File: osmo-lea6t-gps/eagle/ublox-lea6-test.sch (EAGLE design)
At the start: 48 parts, among them U1 UBLOX-LEA-6T, U2 TPS73633, U3 TPS73633, X1 SERIAL, X2 ANT, X3 FOUT, X4 ANT, X5 FOUT, X6 1PPS, X7 PC, X8 1PPS, X9 22-23-2021

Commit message: sylvains branch (ignores some of harald's changes)
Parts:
- added LED1: (no value), led:LEDSML0603
- added R13: (no value), we_passive:R-EU_0603
- added R14: DNP, we_passive:R-EU_0603
- added TP8: TESTPAD, we_conn:TESTPAD
- C10, C6: value 10u -> (none)
- C11, C13, C7, C9: value 1u -> ?
- C12, C8: value 10n -> ?
- D1, D2: value BAT54 -> (none)
- R10: value 1k -> OR
- R12: value DNP -> (none)
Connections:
- new net N$27: LED1.C, R13.2
- new net N$28: R14.1, TP8.TP
- net 3V3: now also LED1.A
- net GND: now also R13.1
- net N$6: now also R14.2
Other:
- moved on the sheet: C6, D2
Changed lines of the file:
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@@
 <?xml version="1.0" encoding="utf-8"?>
 <!DOCTYPE eagle SYSTEM "eagle.dtd">
-<eagle version="6.0">
+<eagle version="6.1">
 <drawing>
 <settings>
@@
 <setting verticaltext="up"/>
 </settings>
-<grid distance="0.1" unitdist="inch" unit="inch" style="lines" multiple="1" display="no" altdistance="0.01" altunitdist="inch" altunit="inch"/>
+<grid distance="0.1" unitdist="inch" unit="inch" style="lines" multiple="1" display="yes" altdistance="0.01" altunitdist="inch" altunit="inch"/>
 <layers>
 <layer number="1" name="Top" color="4" fill="1" visible="no" active="no"/>
@@
 <part name="X9" library="con-molex" deviceset="22-23-2021" device=""/>
 <part name="U$16" library="we_supply" deviceset="GND" device=""/>
-<part name="C12" library="we_passive" deviceset="C-EU" device="_0603" value="10n"/>
-<part name="C13" library="we_passive" deviceset="C-EU" device="_0603" value="1u"/>
-<part name="C11" library="we_passive" deviceset="C-EU" device="_0603" value="1u"/>
+<part name="C12" library="we_passive" deviceset="C-EU" device="_0603" value="?"/>
+<part name="C13" library="we_passive" deviceset="C-EU" device="_0603" value="?"/>
+<part name="C11" library="we_passive" deviceset="C-EU" device="_0603" value="?"/>
 <part name="U$17" library="we_supply" deviceset="GND" device=""/>
 <part name="U$18" library="we_supply" deviceset="GND" device=""/>
 <part name="U$19" library="we_supply" deviceset="GND" device=""/>
-<part name="R10" library="we_passive" deviceset="R-EU" device="_0603" value="1k"/>
+<part name="R10" library="we_passive" deviceset="R-EU" device="_0603" value="OR"/>
 <part name="R11" library="we_passive" deviceset="R-EU" device="_0603" value="DNP"/>
-<part name="C8" library="we_passive" deviceset="C-EU" device="_0603" value="10n"/>
-<part name="C9" library="we_passive" deviceset="C-EU" device="_0603" value="1u"/>
+<part name="C8" library="we_passive" deviceset="C-EU" device="_0603" value="?"/>
+<part name="C9" library="we_passive" deviceset="C-EU" device="_0603" value="?"/>
 <part name="U$20" library="we_supply" deviceset="GND" device=""/>
 <part name="U$21" library="we_supply" deviceset="GND" device=""/>
 <part name="U$22" library="we_supply" deviceset="3V3" device=""/>
-<part name="D1" library="we_passive" deviceset="D_SCHOTTKY" device="_SOT23" value="BAT54"/>
-<part name="D2" library="we_passive" deviceset="D_SCHOTTKY" device="_SOT23" value="BAT54"/>
-<part name="R12" library="we_passive" deviceset="R-EU" device="_0603" value="DNP"/>
+<part name="D1" library="we_passive" deviceset="D_SCHOTTKY" device="_SOT23"/>
+<part name="D2" library="we_passive" deviceset="D_SCHOTTKY" device="_SOT23"/>
+<part name="R12" library="we_passive" deviceset="R-EU" device="_0603"/>
 <part name="U$23" library="we_supply" deviceset="GND" device=""/>
-<part name="C7" library="we_passive" deviceset="C-EU" device="_0603" value="1u"/>
+<part name="C7" library="we_passive" deviceset="C-EU" device="_0603" value="?"/>
 <part name="U$24" library="we_supply" deviceset="GND" device=""/>
 <part name="C1" library="we_passive" deviceset="C-EU" device="_0603" value="100n"/>
@@
 <part name="U$26" library="we_supply" deviceset="GND" device=""/>
 <part name="R7" library="we_passive" deviceset="R-EU" device="_0603" value="0R"/>
-<part name="C6" library="rcl" deviceset="CPOL-EU" device="A/3216-18R" value="10u"/>
+<part name="C6" library="rcl" deviceset="CPOL-EU" device="A/3216-18R"/>
 <part name="U$27" library="we_supply" deviceset="GND" device=""/>
 <part name="R9" library="we_passive" deviceset="R-EU" device="_0603" value="1M"/>
 <part name="C5" library="we_passive" deviceset="C-EU" device="_0603" value="100n"/>
-<part name="C10" library="rcl" deviceset="CPOL-EU" device="A/3216-18R" value="10u"/>
+<part name="C10" library="rcl" deviceset="CPOL-EU" device="A/3216-18R"/>
 <part name="U$28" library="we_supply" deviceset="GND" device=""/>
+<part name="LED1" library="led" deviceset="LED" device="SML0603"/>
+<part name="R13" library="we_passive" deviceset="R-EU" device="_0603"/>
+<part name="TP8" library="we_conn" deviceset="TESTPAD" device=""/>
+<part name="R14" library="we_passive" deviceset="R-EU" device="_0603" value="DNP"/>
+<part name="U$29" library="we_supply" deviceset="GND" device=""/>
 </parts>
 <sheets>
@@
 <instance part="U$18" gate="G$1" x="116.84" y="7.62"/>
 <instance part="U$19" gate="G$1" x="127" y="7.62"/>
-<instance part="R10" gate="SYM" x="81.28" y="68.58"/>
-<instance part="R11" gate="SYM" x="81.28" y="63.5"/>
+<instance part="R10" gate="SYM" x="81.28" y="68.58" smashed="yes">
+<attribute name="NAME" x="76.2" y="72.39" size="1.778" layer="95" rot="MR180"/>
+<attribute name="VALUE" x="83.82" y="72.39" size="1.778" layer="96" rot="MR180"/>
+</instance>
+<instance part="R11" gate="SYM" x="81.28" y="63.5" smashed="yes">
+<attribute name="NAME" x="76.2" y="59.69" size="1.778" layer="95"/>
+<attribute name="VALUE" x="83.82" y="59.69" size="1.778" layer="96"/>
+</instance>
 <instance part="C8" gate="SYM" x="116.84" y="60.96"/>
 <instance part="C9" gate="SYM" x="127" y="60.96"/>
 <instance part="U$20" gate="G$1" x="116.84" y="50.8"/>
 <instance part="U$21" gate="G$1" x="127" y="50.8"/>
-<instance part="U$22" gate="G$1" x="157.48" y="78.74"/>
+<instance part="U$22" gate="G$1" x="175.26" y="78.74"/>
 <instance part="D1" gate="SYM" x="147.32" y="73.66"/>
-<instance part="D2" gate="SYM" x="149.86" y="30.48"/>
+<instance part="D2" gate="SYM" x="147.32" y="30.48"/>
 <instance part="R12" gate="SYM" x="139.7" y="60.96" rot="R90"/>
 <instance part="U$23" gate="G$1" x="139.7" y="50.8"/>
@@
 <instance part="U$26" gate="G$1" x="71.12" y="99.06"/>
 <instance part="R7" gate="SYM" x="218.44" y="109.22"/>
-<instance part="C6" gate="G$1" x="165.1" y="66.04"/>
-<instance part="U$27" gate="G$1" x="165.1" y="55.88"/>
+<instance part="C6" gate="G$1" x="160.02" y="60.96"/>
+<instance part="U$27" gate="G$1" x="160.02" y="45.72"/>
 <instance part="R9" gate="SYM" x="27.94" y="71.12" rot="R90"/>
 <instance part="C5" gate="SYM" x="33.02" y="72.39"/>
 <instance part="C10" gate="G$1" x="73.66" y="20.32"/>
 <instance part="U$28" gate="G$1" x="73.66" y="7.62" rot="MR0"/>
+<instance part="LED1" gate="G$1" x="170.18" y="68.58"/>
+<instance part="R13" gate="SYM" x="170.18" y="55.88" rot="R90"/>
+<instance part="TP8" gate="TP" x="55.88" y="137.16" smashed="yes" rot="R90">
+<attribute name="NAME" x="45.72" y="134.62" size="1.778" layer="95"/>
+</instance>
+<instance part="R14" gate="SYM" x="63.5" y="137.16"/>
+<instance part="U$29" gate="G$1" x="170.18" y="45.72"/>
 </instances>
 <busses>
@@
 <pinref part="C6" gate="G$1" pin="-"/>
 <pinref part="U$27" gate="G$1" pin="GND"/>
-<wire x1="165.1" y1="60.96" x2="165.1" y2="58.42" width="0.1524" layer="91"/>
+<wire x1="160.02" y1="55.88" x2="160.02" y2="48.26" width="0.1524" layer="91"/>
 </segment>
 <segment>
@@
 <pinref part="U$28" gate="G$1" pin="GND"/>
 </segment>
+<segment>
+<pinref part="R13" gate="SYM" pin="1"/>
+<pinref part="U$29" gate="G$1" pin="GND"/>
+<wire x1="170.18" y1="50.8" x2="170.18" y2="48.26" width="0.1524" layer="91"/>
+</segment>
 </net>
 <net name="1PPS" class="0">
@@
 <pinref part="U1" gate="SYM" pin="V_ANT"/>
 <wire x1="71.12" y1="137.16" x2="88.9" y2="137.16" width="0.1524" layer="91"/>
+<pinref part="R14" gate="SYM" pin="2"/>
+<wire x1="68.58" y1="137.16" x2="71.12" y2="137.16" width="0.1524" layer="91"/>
+<junction x="71.12" y="137.16"/>
 </segment>
 </net>
@@
 </segment>
 <segment>
+<pinref part="D2" gate="SYM" pin="C"/>
+<wire x1="154.94" y1="73.66" x2="154.94" y2="30.48" width="0.1524" layer="91"/>
+<wire x1="154.94" y1="30.48" x2="152.4" y2="30.48" width="0.1524" layer="91"/>
+<pinref part="D1" gate="SYM" pin="C"/>
+<wire x1="154.94" y1="73.66" x2="152.4" y2="73.66" width="0.1524" layer="91"/>
+<junction x="154.94" y="73.66"/>
+<wire x1="154.94" y1="73.66" x2="160.02" y2="73.66" width="0.1524" layer="91"/>
+<pinref part="C6" gate="G$1" pin="+"/>
+<wire x1="160.02" y1="73.66" x2="160.02" y2="63.5" width="0.1524" layer="91"/>
+<pinref part="LED1" gate="G$1" pin="A"/>
+<wire x1="160.02" y1="73.66" x2="170.18" y2="73.66" width="0.1524" layer="91"/>
+<wire x1="170.18" y1="73.66" x2="170.18" y2="71.12" width="0.1524" layer="91"/>
+<junction x="160.02" y="73.66"/>
+<wire x1="170.18" y1="73.66" x2="175.26" y2="73.66" width="0.1524" layer="91"/>
+<junction x="170.18" y="73.66"/>
 <pinref part="U$22" gate="G$1" pin="3V3"/>
-<wire x1="157.48" y1="76.2" x2="157.48" y2="73.66" width="0.1524" layer="91"/>
-<pinref part="D2" gate="SYM" pin="C"/>
-<wire x1="157.48" y1="73.66" x2="157.48" y2="30.48" width="0.1524" layer="91"/>
-<wire x1="157.48" y1="30.48" x2="154.94" y2="30.48" width="0.1524" layer="91"/>
-<pinref part="D1" gate="SYM" pin="C"/>
-<wire x1="157.48" y1="73.66" x2="152.4" y2="73.66" width="0.1524" layer="91"/>
-<junction x="157.48" y="73.66"/>
-<wire x1="157.48" y1="73.66" x2="165.1" y2="73.66" width="0.1524" layer="91"/>
-<pinref part="C6" gate="G$1" pin="+"/>
-<wire x1="165.1" y1="73.66" x2="165.1" y2="68.58" width="0.1524" layer="91"/>
+<wire x1="175.26" y1="73.66" x2="175.26" y2="76.2" width="0.1524" layer="91"/>
 </segment>
 </net>
@@
 <wire x1="114.3" y1="30.48" x2="127" y2="30.48" width="0.1524" layer="91"/>
 <pinref part="C13" gate="SYM" pin="1"/>
-<wire x1="127" y1="30.48" x2="144.78" y2="30.48" width="0.1524" layer="91"/>
+<wire x1="127" y1="30.48" x2="142.24" y2="30.48" width="0.1524" layer="91"/>
 <wire x1="127" y1="20.32" x2="127" y2="30.48" width="0.1524" layer="91"/>
 <junction x="127" y="30.48"/>
@@
 </segment>
 </net>
+<net name="N$27" class="0">
+<segment>
+<pinref part="LED1" gate="G$1" pin="C"/>
+<pinref part="R13" gate="SYM" pin="2"/>
+<wire x1="170.18" y1="63.5" x2="170.18" y2="60.96" width="0.1524" layer="91"/>
+</segment>
+</net>
+<net name="N$28" class="0">
+<segment>
+<pinref part="TP8" gate="TP" pin="TP"/>
+<pinref part="R14" gate="SYM" pin="1"/>
+<wire x1="55.88" y1="137.16" x2="58.42" y2="137.16" width="0.1524" layer="91"/>
+</segment>
+</net>

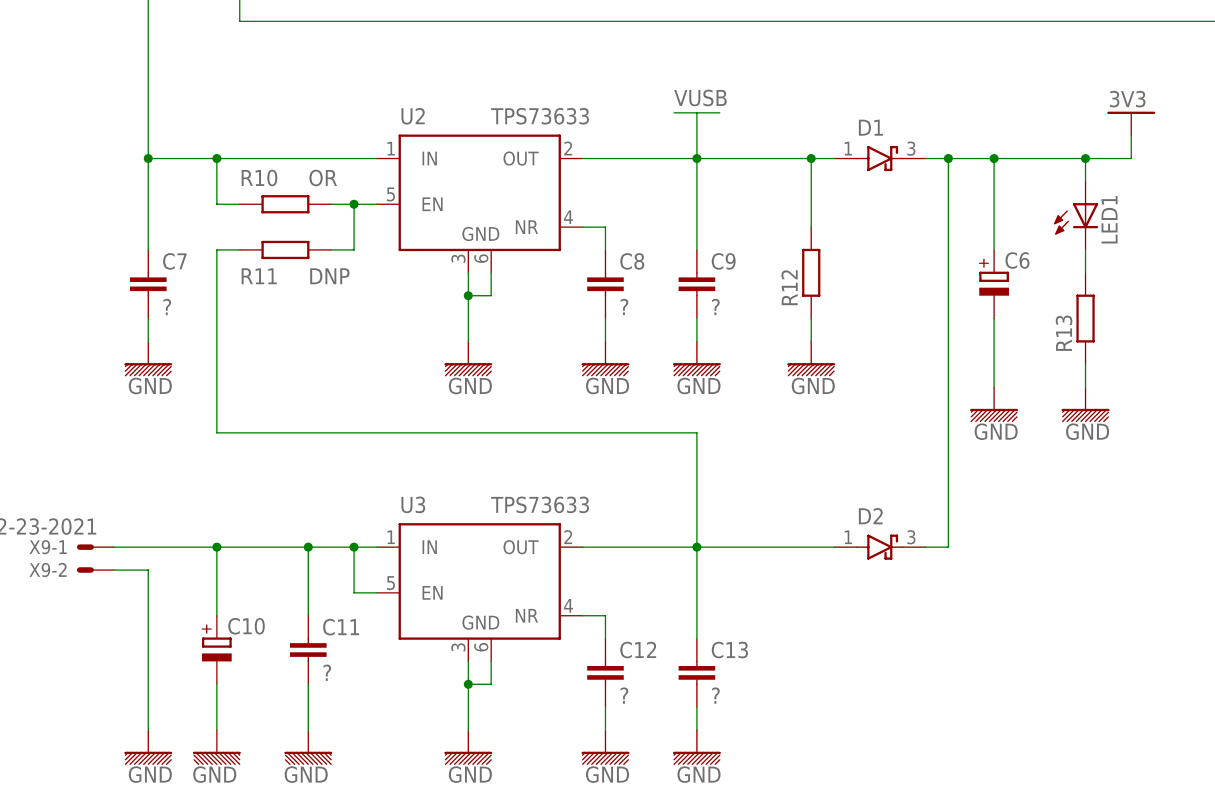
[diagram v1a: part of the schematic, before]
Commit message: re-merge my previous changes manually into the project
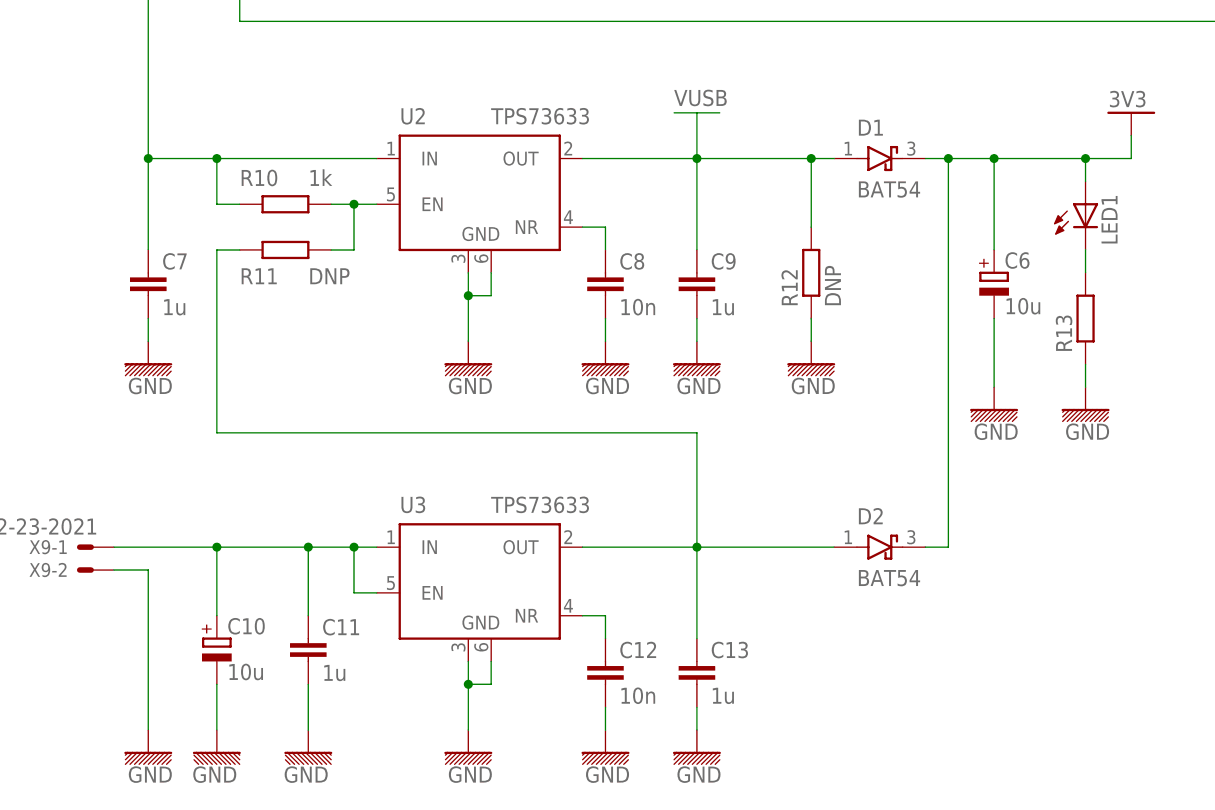
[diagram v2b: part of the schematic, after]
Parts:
- C10, C6: value (none) -> 10u
- C11, C13, C7, C9: value ? -> 1u
- C12, C8: value ? -> 10n
- D1, D2: value (none) -> BAT54
- R10: value OR -> 1k
- R12: value (none) -> DNP
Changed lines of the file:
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@@
 <part name="X9" library="con-molex" deviceset="22-23-2021" device=""/>
 <part name="U$16" library="we_supply" deviceset="GND" device=""/>
-<part name="C12" library="we_passive" deviceset="C-EU" device="_0603" value="?"/>
-<part name="C13" library="we_passive" deviceset="C-EU" device="_0603" value="?"/>
-<part name="C11" library="we_passive" deviceset="C-EU" device="_0603" value="?"/>
+<part name="C12" library="we_passive" deviceset="C-EU" device="_0603" value="10n"/>
+<part name="C13" library="we_passive" deviceset="C-EU" device="_0603" value="1u"/>
+<part name="C11" library="we_passive" deviceset="C-EU" device="_0603" value="1u"/>
 <part name="U$17" library="we_supply" deviceset="GND" device=""/>
 <part name="U$18" library="we_supply" deviceset="GND" device=""/>
 <part name="U$19" library="we_supply" deviceset="GND" device=""/>
-<part name="R10" library="we_passive" deviceset="R-EU" device="_0603" value="OR"/>
+<part name="R10" library="we_passive" deviceset="R-EU" device="_0603" value="1k"/>
 <part name="R11" library="we_passive" deviceset="R-EU" device="_0603" value="DNP"/>
-<part name="C8" library="we_passive" deviceset="C-EU" device="_0603" value="?"/>
-<part name="C9" library="we_passive" deviceset="C-EU" device="_0603" value="?"/>
+<part name="C8" library="we_passive" deviceset="C-EU" device="_0603" value="10n"/>
+<part name="C9" library="we_passive" deviceset="C-EU" device="_0603" value="1u"/>
 <part name="U$20" library="we_supply" deviceset="GND" device=""/>
 <part name="U$21" library="we_supply" deviceset="GND" device=""/>
 <part name="U$22" library="we_supply" deviceset="3V3" device=""/>
-<part name="D1" library="we_passive" deviceset="D_SCHOTTKY" device="_SOT23"/>
-<part name="D2" library="we_passive" deviceset="D_SCHOTTKY" device="_SOT23"/>
-<part name="R12" library="we_passive" deviceset="R-EU" device="_0603"/>
+<part name="D1" library="we_passive" deviceset="D_SCHOTTKY" device="_SOT23" value="BAT54"/>
+<part name="D2" library="we_passive" deviceset="D_SCHOTTKY" device="_SOT23" value="BAT54"/>
+<part name="R12" library="we_passive" deviceset="R-EU" device="_0603" value="DNP"/>
 <part name="U$23" library="we_supply" deviceset="GND" device=""/>
-<part name="C7" library="we_passive" deviceset="C-EU" device="_0603" value="?"/>
+<part name="C7" library="we_passive" deviceset="C-EU" device="_0603" value="1u"/>
 <part name="U$24" library="we_supply" deviceset="GND" device=""/>
 <part name="C1" library="we_passive" deviceset="C-EU" device="_0603" value="100n"/>
@@
 <part name="U$26" library="we_supply" deviceset="GND" device=""/>
 <part name="R7" library="we_passive" deviceset="R-EU" device="_0603" value="0R"/>
-<part name="C6" library="rcl" deviceset="CPOL-EU" device="A/3216-18R"/>
+<part name="C6" library="rcl" deviceset="CPOL-EU" device="A/3216-18R" value="10u"/>
 <part name="U$27" library="we_supply" deviceset="GND" device=""/>
 <part name="R9" library="we_passive" deviceset="R-EU" device="_0603" value="1M"/>
 <part name="C5" library="we_passive" deviceset="C-EU" device="_0603" value="100n"/>
-<part name="C10" library="rcl" deviceset="CPOL-EU" device="A/3216-18R"/>
+<part name="C10" library="rcl" deviceset="CPOL-EU" device="A/3216-18R" value="10u"/>
 <part name="U$28" library="we_supply" deviceset="GND" device=""/>
 <part name="LED1" library="led" deviceset="LED" device="SML0603"/>
